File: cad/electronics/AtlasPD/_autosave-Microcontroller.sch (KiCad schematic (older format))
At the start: 32 parts, among them J201 USB_C_Receptacle_USB2.0, J202 Conn_01x04, SW201 SW_SPST, U201 CP2104, U202 ATmega328P-AU, Y201 CSTNE16M0V53-R0

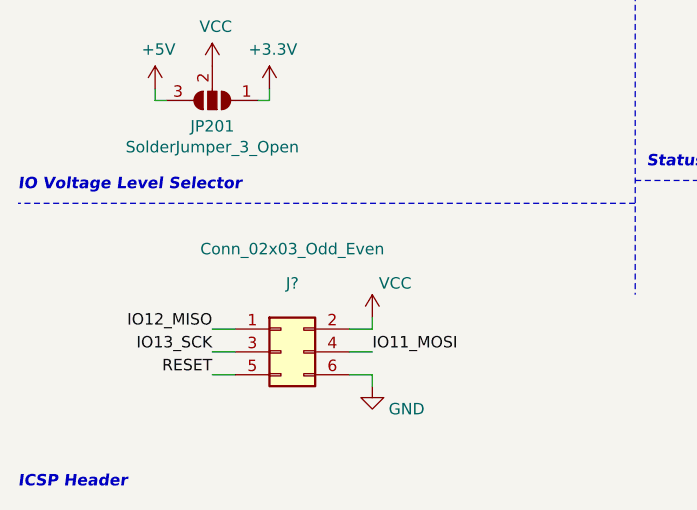
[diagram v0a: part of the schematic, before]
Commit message: Chaning MCU board size for better layout
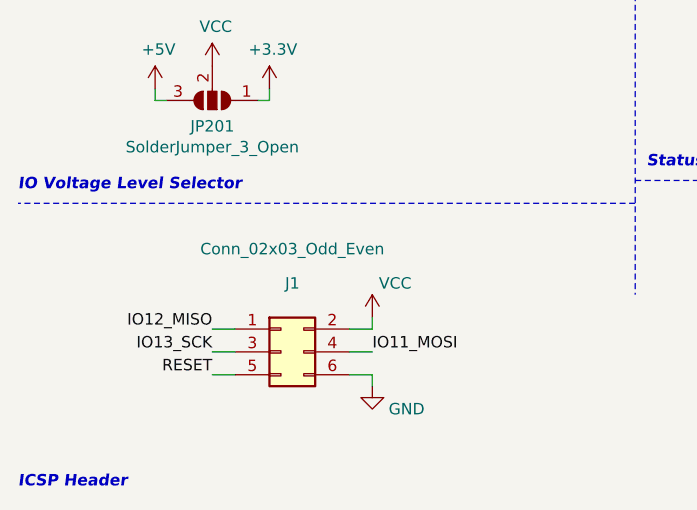
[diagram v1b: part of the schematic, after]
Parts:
- J1: renamed from J?; footprint (none) -> Connector_PinHeader_2.54mm:PinHeader_2x03_P2.54mm_Vertical
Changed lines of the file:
@@
 Unused MCU pins
 $Comp
-L Connector_Generic:Conn_02x03_Odd_Even J?
+L Connector_Generic:Conn_02x03_Odd_Even J1
 U 1 1 61A6FF2A
 P 1650 7100
-F 0 "J?" H 1700 7400 50  0000 C CNN
+F 0 "J1" H 1700 7400 50  0000 C CNN
 F 1 "Conn_02x03_Odd_Even" H 1700 7550 50  0000 C CNN
-F 2 "" H 1650 7100 50  0001 C CNN
+F 2 "Connector_PinHeader_2.54mm:PinHeader_2x03_P2.54mm_Vertical" H 1650 7100 50  0001 C CNN
 F 3 "~" H 1650 7100 50  0001 C CNN
 	1    1650 7100
